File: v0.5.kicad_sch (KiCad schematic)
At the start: 61 parts, among them J1 USB_B_Micro, J2 Conn_02x06_Odd_Even, J3 Screw_Terminal_01x08, J4 Screw_Terminal_01x04, J5 Conn_Coaxial_Small, Q1 MMBT3904, Q2 SiS454DN, Q3 SiS454DN, Q4 SiS454DN, Q5 SiS454DN, U1 MS5611-01BA, U2 L7805, U3 ACS711xLCTR-25AB, U4 ICM-42670-P, U5 SAM-M10Q-0-10, U6 ADXL375BCCZ, U7 Teensy4.1, U8 RFM69W

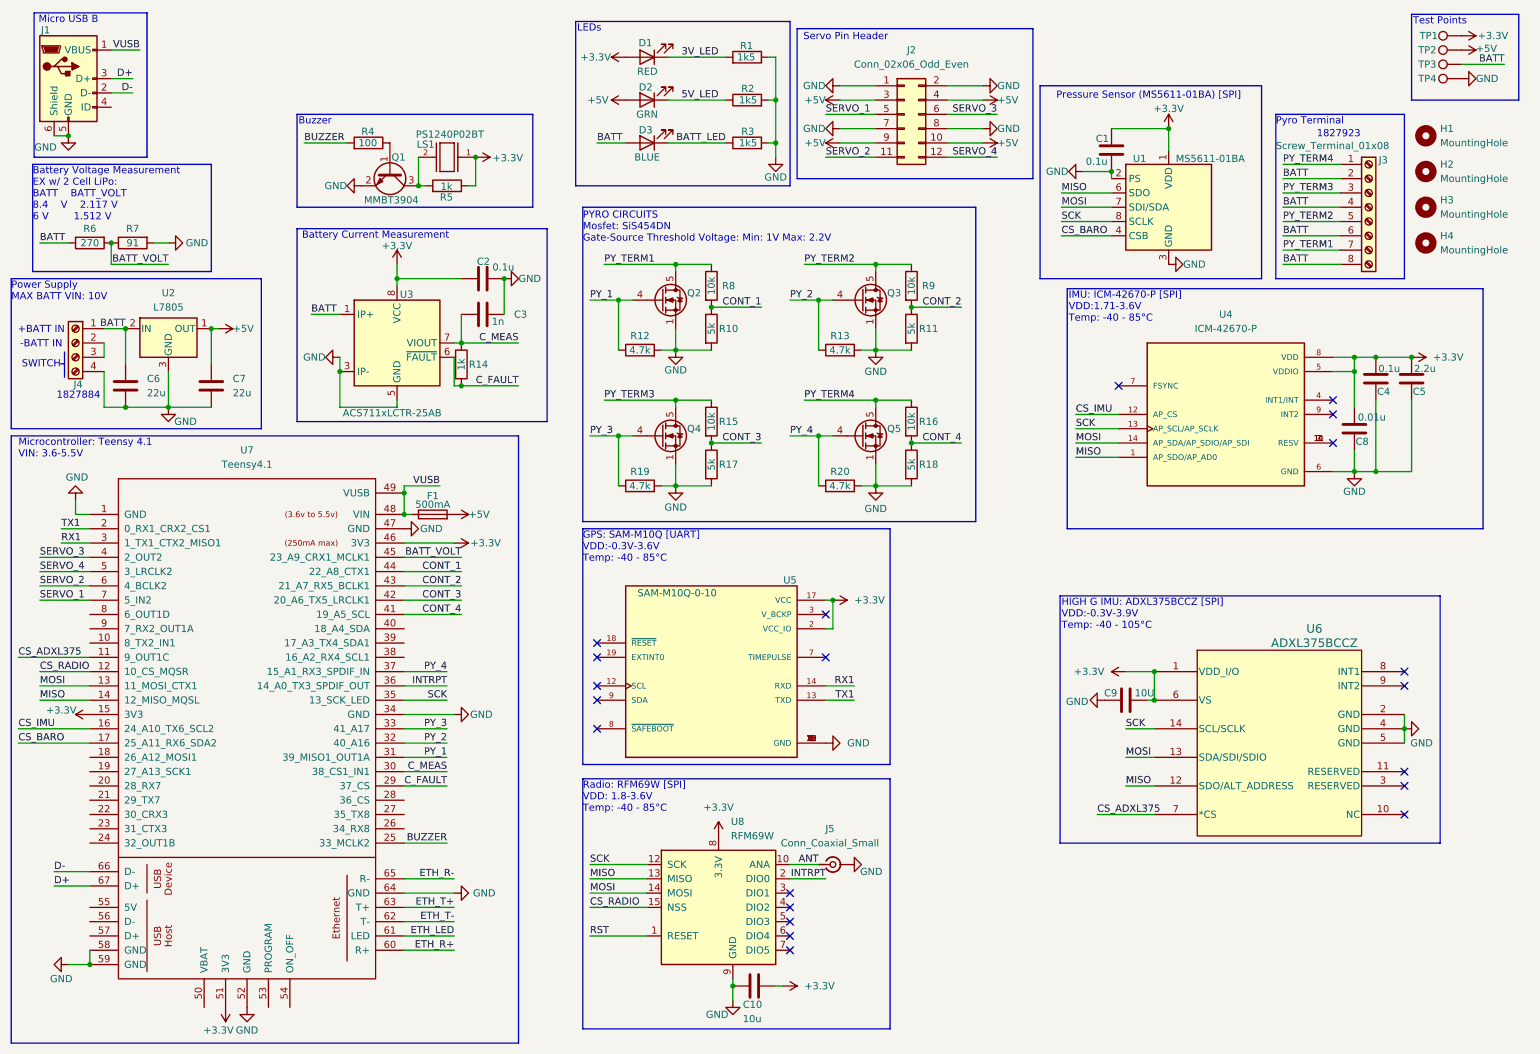
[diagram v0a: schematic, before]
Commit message: Added test pin headers. Updated BOM
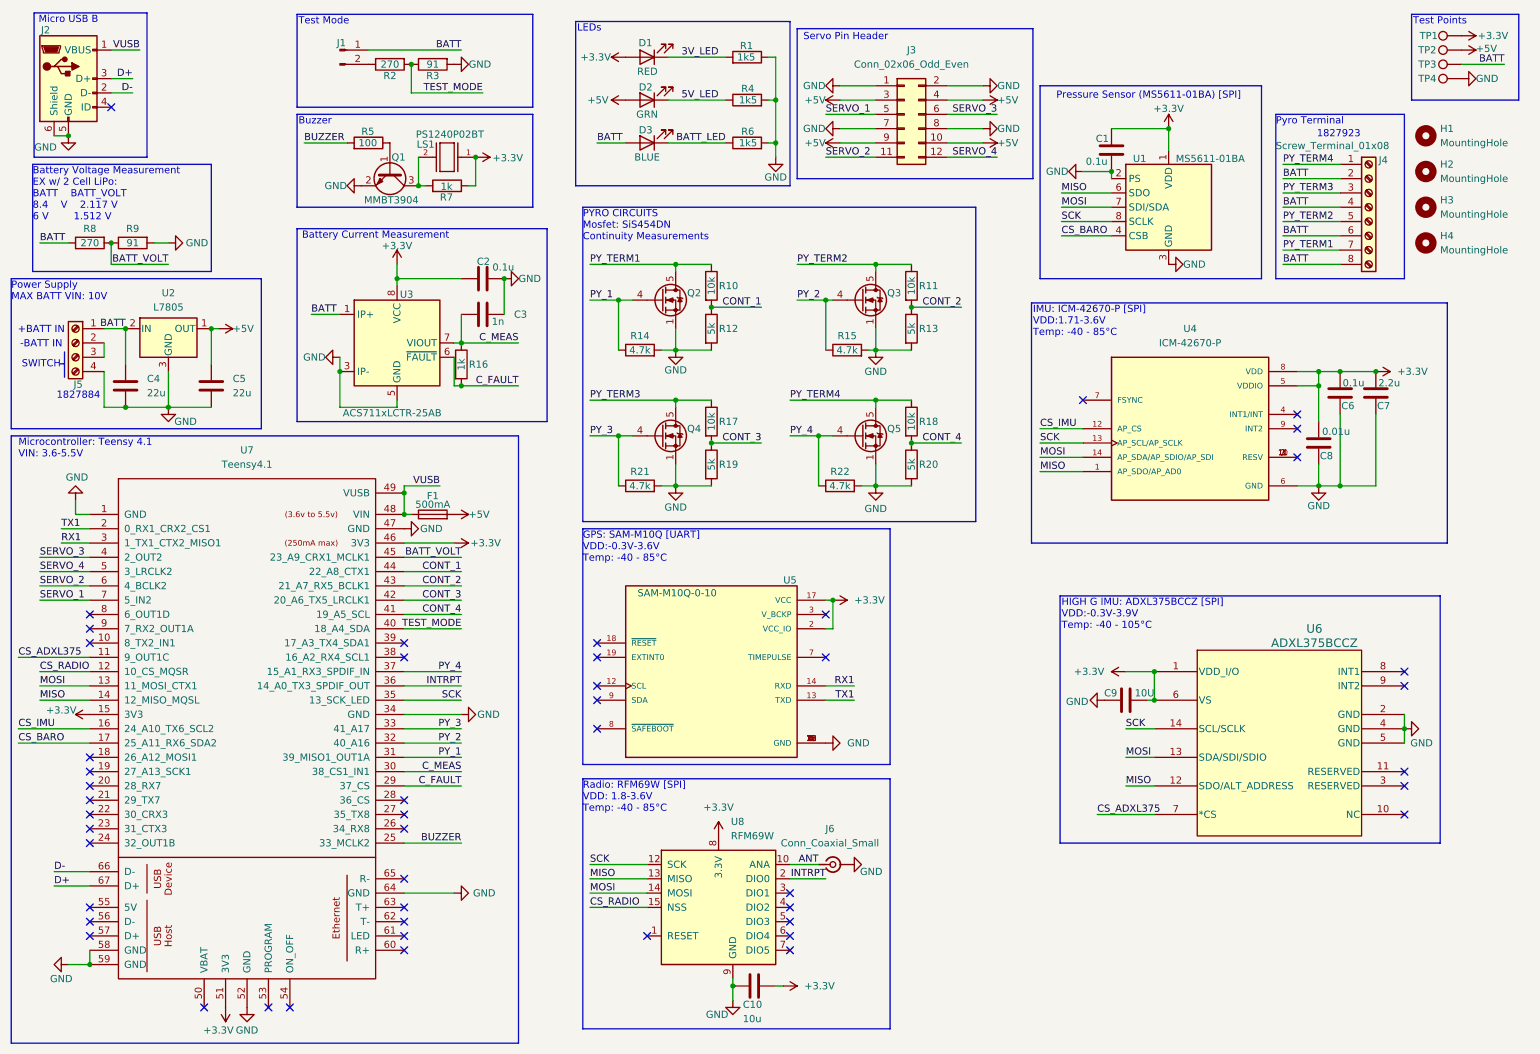
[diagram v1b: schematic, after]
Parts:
- added J1: Conn_01x02_Pin, Connector_PinHeader_1.27mm:PinHeader_1x02_P1.27mm_Horizontal, symbol Connector:Conn_01x02_Pin
- added R2: 270, Resistor_SMD:R_0805_2012Metric, symbol Device:R
- added R3: 91, Resistor_SMD:R_0805_2012Metric, symbol Device:R
- renumbered C6 to C4, C7 to C5, C4 to C6, C5 to C7, J1 to J2, J2 to J3, J3 to J4, J4 to J5, J5 to J6, R8 to R10, R9 to R11, R10 to R12, R11 to R13, R12 to R14, R13 to R15, R14 to R16, R15 to R17, R16 to R18, R17 to R19, R18 to R20, R19 to R21, R20 to R22, R2 to R4, R4 to R5, R3 to R6, R5 to R7, R6 to R8, R7 to R9
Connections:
- net BATT: now also J1.1 (Pin_1)
- net GND: now also R3.2
- net TEST_MODE: now reaches U7.40 (18_A4_SDA)
- net TEST_MODE: now also R2.2, R3.1
- net ETH_LED: no longer names the net of U7.61 (LED)
- net ETH_R+: no longer names the net of U7.60 (R+)
- net ETH_R-: no longer names the net of U7.65 (R-)
- net ETH_T+: no longer names the net of U7.63 (T+)
- net ETH_T-: no longer names the net of U7.62 (T-)
- net RST: no longer names the net of U8.1 (RESET)
- new net: J1.2 (Pin_2), R2.1
- no-connect marks 21 -> 49
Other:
- note added: "PYRO CIRCUITS Mosfet: SiS454DN Continuity Measurements"
- note added: "Test Mode"
- note removed: "PYRO CIRCUITS Mosfet: SiS454DN Gate-Source Threshold Voltage: Min: 1V Max: 2.2V"
- moved on the sheet: C6, C7, C8, R15, U4

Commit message: Using RFM95W radio now instead of RFM69W.
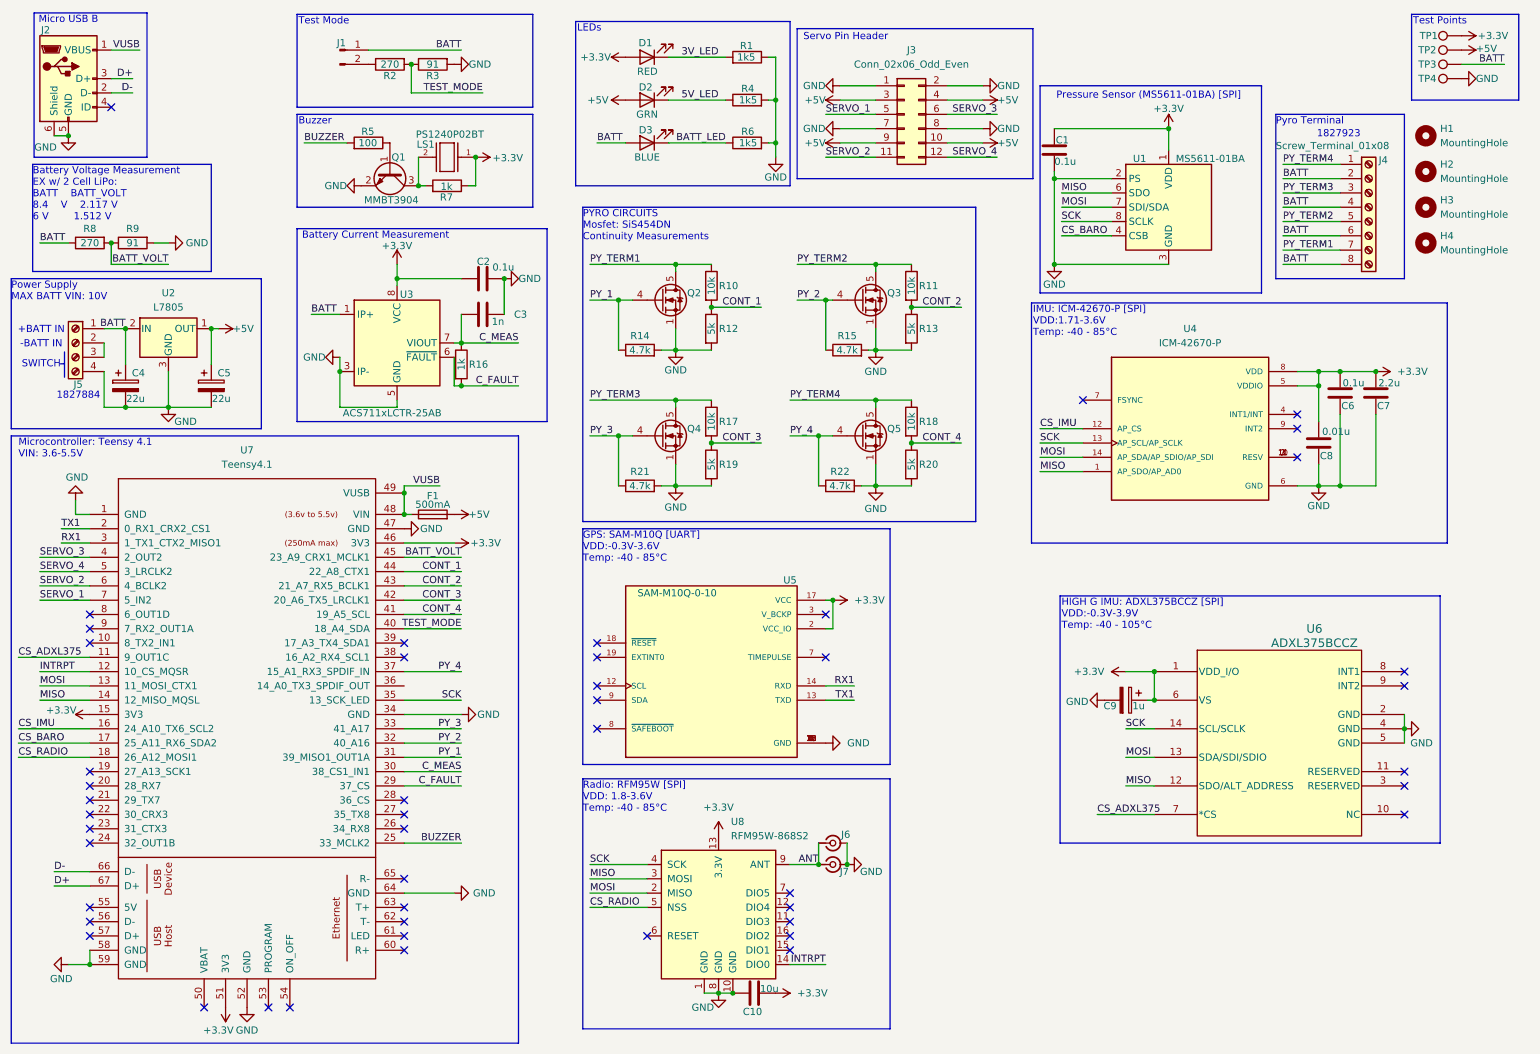
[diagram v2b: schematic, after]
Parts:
- removed C4, C5: 22u, Capacitor_SMD:C_0805_2012Metric_Pad1.18x1.45mm_HandSolder, symbol Device:C
- removed C9: 10U, Capacitor_SMD:C_0805_2012Metric, symbol Device:C
- removed U8: RFM69W, RF_Module:HOPERF_RFM69HW, symbol RF_Module:RFM69W
- added C4, C5: 22u, Capacitor_SMD:C_0805_2012Metric, symbol Device:C_Polarized
- added C9: 1u, Capacitor_SMD:C_0805_2012Metric, symbol Device:C_Polarized
- added J6: Conn_Coaxial_Small, Connector_Coaxial:U.FL_Hirose_U.FL-R-SMT-1_Vertical, symbol Connector:Conn_Coaxial_Small
- added U8: RFM95W-868S2, RF_Module:HOPERF_RFM9XW_SMD, symbol RF_Module:RFM95W-868S2
- renumbered J6 to J7
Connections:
- net +3.3V: now also C9.1, U8.13 (3.3V)
- net +5V: now also C5.1
- net ANT: now also J6.1 (In), U8.9 (ANT)
- net BATT: now also C4.1
- net CS_RADIO: now also U7.18 (26_A12_MOSI1), U8.5 (NSS); no longer U7.12 (10_CS_MQSR)
- net GND: now also C4.2, C5.2, C9.2, J6.2 (Ext), U8.1 (GND), U8.10 (GND), U8.8 (GND)
- net MISO: now also U8.3 (MOSI)
- net MOSI: now also U8.2 (MISO)
- net SCK: now also U8.4 (SCK)
- net  INTRPT: no longer names the net of U7.36 (14_A0_TX3_SPDIF_OUT)
- new net INTRPT: U7.12 (10_CS_MQSR), U8.14 (DIO0)
- no-connect marks 49 -> 48
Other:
- note added: "Radio: RFM95W [SPI] VDD: 1.8-3.6V Temp: -40 - 85°C"
- note removed: "Radio: RFM69W [SPI] VDD: 1.8-3.6V Temp: -40 - 85°C"
- moved on the sheet: C1, C10

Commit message: Updated gerber files
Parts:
- C4, C5: DigiKey TAJR105K010RNJ -> TLJN226M010R3800
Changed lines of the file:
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@@
 			)
 		)
-		(property "DigiKey" "TAJR105K010RNJ"
+		(property "DigiKey" "TLJN226M010R3800"
 			(at 33.02 80.01 90)
 			(effects
@@
 			)
 		)
-		(property "DigiKey" "TAJR105K010RNJ"
+		(property "DigiKey" "TLJN226M010R3800"
 			(at 48.26 80.01 90)
 			(effects
